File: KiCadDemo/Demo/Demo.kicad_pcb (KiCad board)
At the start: 4 copper layers, 100 x 80 mm, 66 parts, among them J1 Power, J2 22-05-7025, J3 22-05-7025, J4 22-05-7025, J5 22-05-7025, J6 Comm, J7 USB_B_Mini, J8 Debug, M1 BSS84, M2 BSS84, SW1 Reset, U1 TSR_1-2450, U2 UA78M33, U3 STM32F103CBT6, U4 DS1822-PAR, U5 MAX3486, U6 74LS06, X1 8 MHz

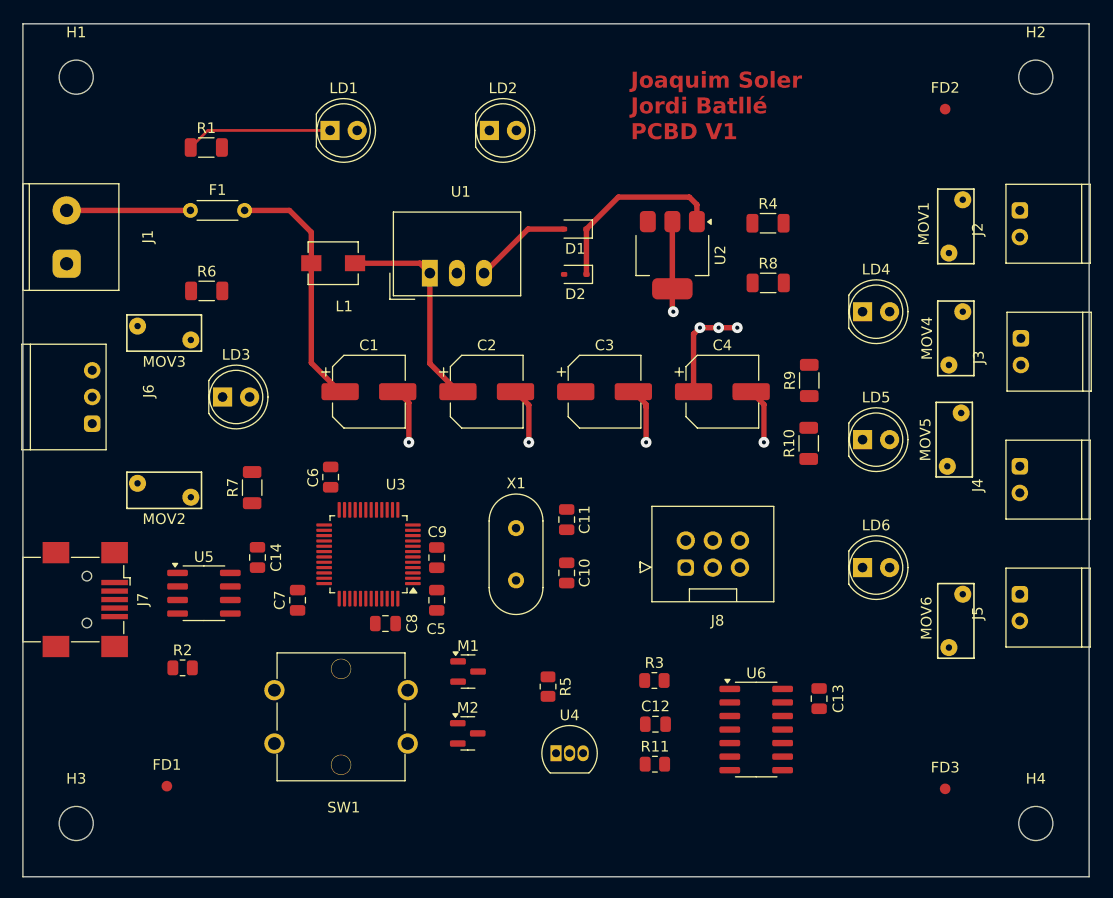
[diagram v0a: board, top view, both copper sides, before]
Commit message: Moodify component names and text label
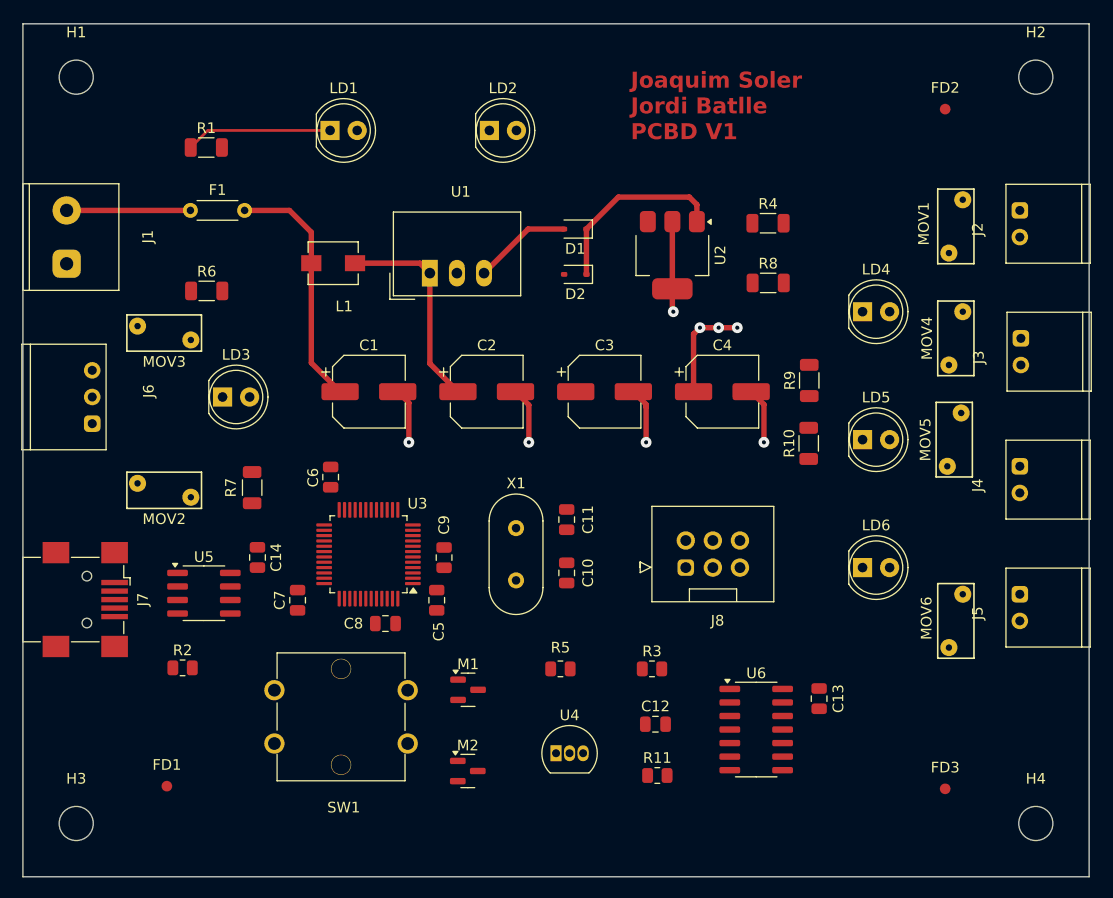
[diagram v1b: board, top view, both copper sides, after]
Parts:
- moved M2 3.53 mm to (141.7, 120.1)
- moved R5 2.03 mm to (150.4, 110.5), turned to 180 degrees
- moved M1 1.71 mm to (141.8, 112.5)
- moved R3 1.11 mm to (159.0, 110.5)
- moved R11 1.08 mm to (159.5, 120.5)
- moved C9 0.69 mm to (139.5, 100.1)
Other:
- board text added: "Joaquim Soler Jordi Batlle PCBD V1"
- board text removed: "Joaquim Soler Jordi Batllé PCBD V1"
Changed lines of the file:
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@@
   )
   (footprint "Capacitor_SMD:C_0805_2012Metric" (layer "F.Cu")
-    (at 138.8125 100.0625 90)
+    (at 139.5 100.0625 90)
     (descr "Capacitor SMD 0805 (2012 Metric), square (rectangular) end terminal, IPC_7351 nominal, (Body size source: IPC-SM-782 page 76, https://www.pcb-3d.com/wordpress/wp-content/uploads/ipc-sm-782a_amendment_1_and_2.pdf, https://docs.google.com/spreadsheets/d/1BsfQQcO9C6DZCsRaXUlFlo91Tg2WpOkGARC1WS5S8t0/edit?usp=sharing), generated with kicad-footprint-generator")
     (tags "capacitor")
@@
     (property "ki_keywords" "cap capacitor")
     (attr smd)
-    (fp_text reference "C9" (at 2.4 0.05 180) (layer "F.SilkS")
+    (fp_text reference "C9" (at 3.0625 0 270) (layer "F.SilkS")
         (effects (font (size 1 1) (thickness 0.15)))
     )
-    (fp_text value "100 nF" (at 0 1.68 90) (layer "F.Fab")
+    (fp_text value "100 nF" (at 4.5625 1.5 90) (layer "F.Fab")
         (effects (font (size 1 1) (thickness 0.15)))
     )
@@
     (property "ki_keywords" "Arm Cortex-M3 STM32F1 STM32F103")
     (attr smd)
-    (fp_text reference "U3" (at -2.55 6.5375) (layer "F.SilkS")
+    (fp_text reference "U3" (at -4.5875 4.75) (layer "F.SilkS")
         (effects (font (size 1 1) (thickness 0.15)))
     )
@@
   )
   (footprint "Resistor_SMD:R_0805_2012Metric" (layer "F.Cu")
-    (at 159.275 119.44)
+    (at 159.5 120.5)
     (descr "Resistor SMD 0805 (2012 Metric), square (rectangular) end terminal, IPC_7351 nominal, (Body size source: IPC-SM-782 page 72, https://www.pcb-3d.com/wordpress/wp-content/uploads/ipc-sm-782a_amendment_1_and_2.pdf), generated with kicad-footprint-generator")
     (tags "resistor")
@@
     (property "ki_keywords" "R res resistor")
     (attr smd)
-    (fp_text reference "R7" (at 0 -1.82 90) (layer "F.SilkS")
+    (fp_text reference "R7" (at 0 -2 90) (layer "F.SilkS")
         (effects (font (size 1 1) (thickness 0.15)))
     )
-    (fp_text value "120R" (at 0 1.82 90) (layer "F.Fab")
+    (fp_text value "120R" (at 0 2 90) (layer "F.Fab")
         (effects (font (size 1 1) (thickness 0.15)))
     )
@@
     (property "ki_keywords" "cap capacitor")
     (attr smd)
-    (fp_text reference "C5" (at -2.7 -0.05 180) (layer "F.SilkS")
+    (fp_text reference "C5" (at -2.9375 0.1875 270) (layer "F.SilkS")
         (effects (font (size 1 1) (thickness 0.15)))
     )
-    (fp_text value "100 nF" (at 0 1.68 90) (layer "F.Fab")
+    (fp_text value "100 nF" (at -1.4375 2.1875 90) (layer "F.Fab")
         (effects (font (size 1 1) (thickness 0.15)))
     )
-    (fp_text user "${REFERENCE}" (at 0 0 90) (layer "F.Fab")
+    (fp_text user "${REFERENCE}" (at 0 0.625 90) (layer "F.Fab")
         (effects (font (size 0.5 0.5) (thickness 0.08)))
     )
@@
     (property "ki_keywords" "cap capacitor")
     (attr smd)
-    (fp_text reference "C10" (at 0 -1.68 90) (layer "F.SilkS")
+    (fp_text reference "C10" (at 0 -2 90) (layer "F.SilkS")
         (effects (font (size 1 1) (thickness 0.15)))
     )
-    (fp_text value "20 pF" (at 0 1.68 90) (layer "F.Fab")
+    (fp_text value "20 pF" (at 0 -3.5 90) (layer "F.Fab")
         (effects (font (size 1 1) (thickness 0.15)))
     )
@@
     (property "ki_keywords" "cap capacitor")
     (attr smd)
-    (fp_text reference "C8" (at 2.5 0 90) (layer "F.SilkS")
+    (fp_text reference "C8" (at -3 0 180) (layer "F.SilkS")
         (effects (font (size 1 1) (thickness 0.15)))
     )
@@
   )
   (footprint "Package_TO_SOT_SMD:SOT-23" (layer "F.Cu")
-    (at 141.75 110.75)
+    (at 141.75 112.46)
     (descr "SOT, 3 Pin (https://www.jedec.org/system/files/docs/to-236h.pdf variant AB), generated with kicad-footprint-generator ipc_gullwing_generator.py")
     (tags "SOT TO_SOT_SMD")
@@
   )
   (footprint "Resistor_SMD:R_0805_2012Metric" (layer "F.Cu")
-    (at 159.225 111.59)
+    (at 159 110.5)
     (descr "Resistor SMD 0805 (2012 Metric), square (rectangular) end terminal, IPC_7351 nominal, (Body size source: IPC-SM-782 page 72, https://www.pcb-3d.com/wordpress/wp-content/uploads/ipc-sm-782a_amendment_1_and_2.pdf), generated with kicad-footprint-generator")
     (tags "resistor")
@@
     (property "ki_keywords" "cap capacitor")
     (attr smd)
-    (fp_text reference "C11" (at 0 -1.68 90) (layer "F.SilkS")
+    (fp_text reference "C11" (at 0 -2 90) (layer "F.SilkS")
         (effects (font (size 1 1) (thickness 0.15)))
     )
-    (fp_text value "20 pF" (at 0 1.68 90) (layer "F.Fab")
+    (fp_text value "20 pF" (at 0 -3.5 90) (layer "F.Fab")
         (effects (font (size 1 1) (thickness 0.15)))
     )
@@
   )
   (footprint "Resistor_SMD:R_0805_2012Metric" (layer "F.Cu")
-    (at 149.25 112.1625 -90)
+    (at 150.4125 110.5 180)
     (descr "Resistor SMD 0805 (2012 Metric), square (rectangular) end terminal, IPC_7351 nominal, (Body size source: IPC-SM-782 page 72, https://www.pcb-3d.com/wordpress/wp-content/uploads/ipc-sm-782a_amendment_1_and_2.pdf), generated with kicad-footprint-generator")
     (tags "resistor")
@@
     (property "ki_keywords" "R res resistor")
     (attr smd)
-    (fp_text reference "R5" (at 0 -1.65 90) (layer "F.SilkS")
+    (fp_text reference "R5" (at 0 2) (layer "F.SilkS")
         (effects (font (size 1 1) (thickness 0.15)))
     )
-    (fp_text value "4k7" (at 0 1.65 90) (layer "F.Fab")
+    (fp_text value "4k7" (at 0 -2) (layer "F.Fab")
         (effects (font (size 1 1) (thickness 0.15)))
     )
-    (fp_text user "${REFERENCE}" (at 0 0.625 90) (layer "F.Fab")
+    (fp_text user "${REFERENCE}" (at 0 0.625) (layer "F.Fab")
         (effects (font (size 0.5 0.5) (thickness 0.08)))
     )
@@
     (fp_line (start 1 0.625) (end -1 0.625)
       (stroke (width 0.1) (type solid)) (layer "F.Fab"))
-    (pad "1" smd roundrect (at -0.9125 0 270) (size 1.025 1.4) (layers "F.Cu" "F.Paste" "F.Mask") (roundrect_rratio 0.243902439)
+    (pad "1" smd roundrect (at -0.9125 0 180) (size 1.025 1.4) (layers "F.Cu" "F.Paste" "F.Mask") (roundrect_rratio 0.243902439)
       (net 6 "+3V3") (pintype "passive"))
-    (pad "2" smd roundrect (at 0.9125 0 270) (size 1.025 1.4) (layers "F.Cu" "F.Paste" "F.Mask") (roundrect_rratio 0.243902439)
+    (pad "2" smd roundrect (at 0.9125 0 180) (size 1.025 1.4) (layers "F.Cu" "F.Paste" "F.Mask") (roundrect_rratio 0.243902439)
       (net 13 "DQ") (pintype "passive"))
     (model "${KICAD6_3DMODEL_DIR}/Resistor_SMD.3dshapes/R_0805_2012Metric.wrl"
@@
   )
   (footprint "Package_TO_SOT_SMD:SOT-23" (layer "F.Cu")
-    (at 141.725 116.55)
+    (at 141.725 120.08)
     (descr "SOT, 3 Pin (https://www.jedec.org/system/files/docs/to-236h.pdf variant AB), generated with kicad-footprint-generator ipc_gullwing_generator.py")
     (tags "SOT TO_SOT_SMD")
@@
   (gr_line (start 100 130) (end 200 130)
     (stroke (width 0.05) (type default)) (layer "Edge.Cuts"))
-  (gr_text "Joaquim Soler\nJordi Batllé\nPCBD V1\n" (at 157 61) (layer "F.Cu")
+  (gr_text "Joaquim Soler\nJordi Batlle\nPCBD V1\n" (at 157 61) (layer "F.Cu")
     (effects (font (size 1.5 1.5) (thickness 0.3) bold) (justify left bottom))
   )

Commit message: Add files via upload
Plots generated.
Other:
- board text added: "Jordi Batlle Joaquim Soler PCB Board Demo v1.0"
- board text removed: "Joaquim Soler Jordi Batlle PCBD V1"
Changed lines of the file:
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@@
       (drillshape 0)
       (scaleselection 1)
-      (outputdirectory "")
+      (outputdirectory "Place/")
     )
   )
@@
   (gr_line (start 100 130) (end 200 130)
     (stroke (width 0.05) (type default)) (layer "Edge.Cuts"))
-  (gr_text "Joaquim Soler\nJordi Batlle\nPCBD V1\n" (at 157 61) (layer "F.Cu")
-    (effects (font (size 1.5 1.5) (thickness 0.3) bold) (justify left bottom))
+  (gr_text "Jordi Batlle\nJoaquim Soler\nPCB Board Demo v1.0" (at 154.41 58.54) (layer "F.SilkS")
+    (effects (font (size 1.5 1.5) (thickness 0.2)) (justify left bottom))
   )
   (segment (start 127.04875 81.79875) (end 129.75 84.5) (width 0.508) (layer "F.Cu") (net 1))

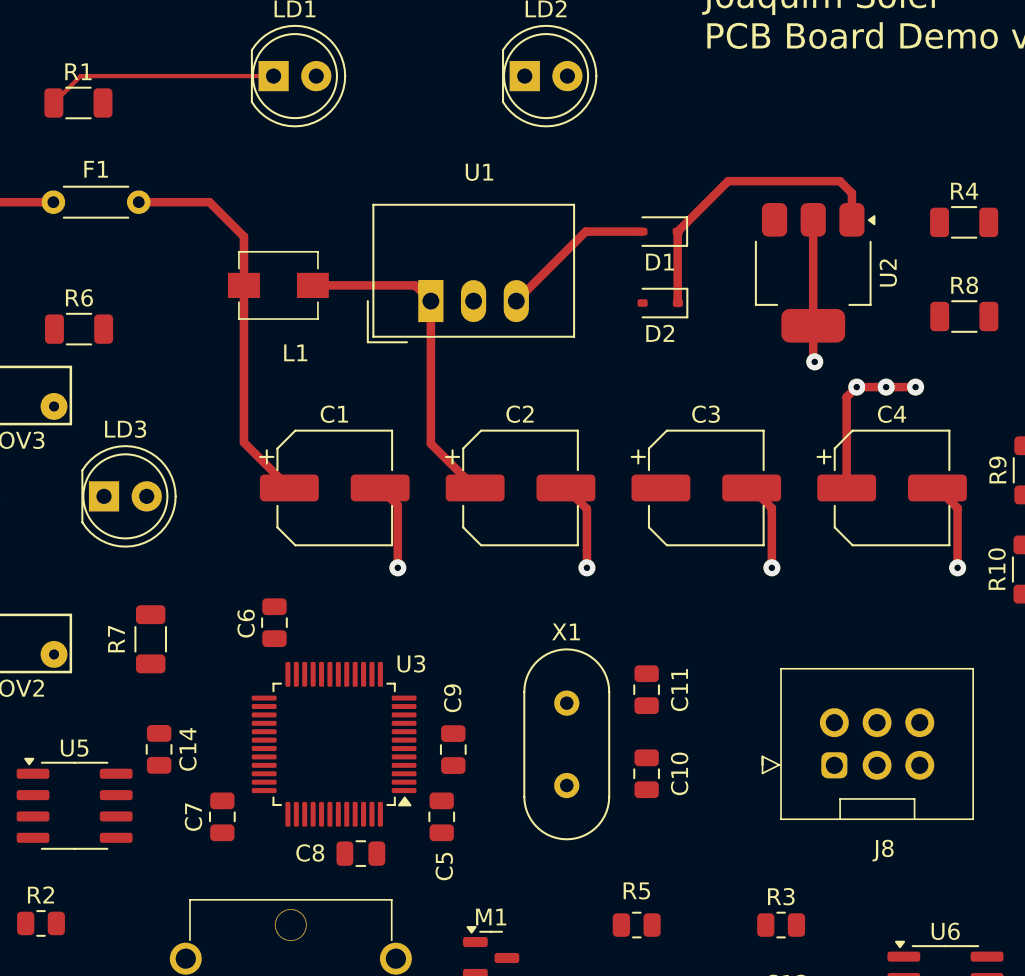
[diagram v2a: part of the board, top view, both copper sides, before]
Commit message: Start of the routing
Power lines routed. MCU coupling capacitors routed and also oscillator.
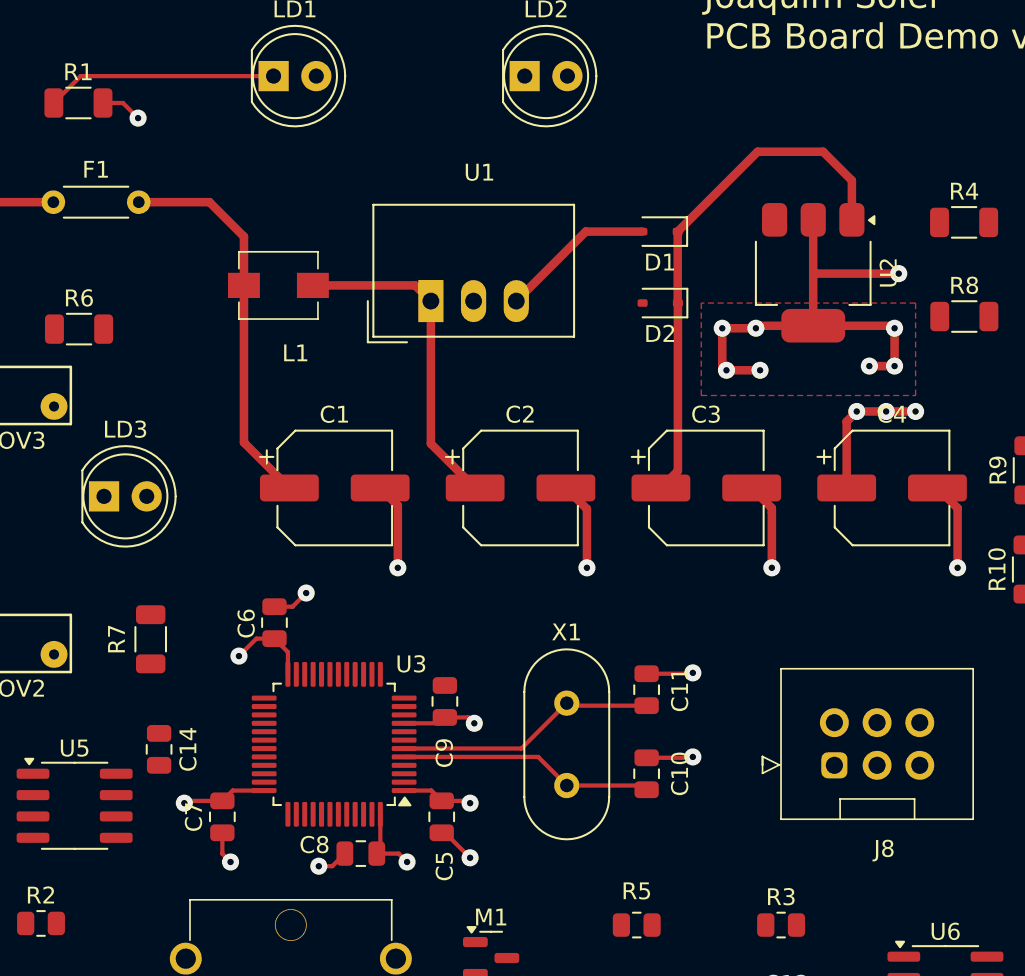
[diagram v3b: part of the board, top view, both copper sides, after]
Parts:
- moved C9 2.91 mm to (139.0, 97.2), turned to -90 degrees
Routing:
- net GND: track 29.9 -> 67.9 mm, vias 5 -> 19
- net +3V3: track 0.00 -> 23.2 mm, vias 0 -> 5
- net Net-(U3-PD1): track 0.00 -> 15.6 mm
- net Net-(U3-PD0): track 0.00 -> 15.2 mm
- net /supply/pwr5: track 17.7 -> 31.1 mm
- net +3.3V: track 9.75 -> 8.30 mm
- added copper zone on F.Cu, net GND

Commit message: Follow routing
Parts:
- moved M2 50.7 mm to (122.8, 73.1), turned to 180 degrees
- moved U5 12.2 mm to (121.0, 91.9), turned to 180 degrees
- moved R7 7.47 mm to (114.2, 92.1)
- moved MOV2 7.00 mm to (103.8, 93.8)
- moved LD3 4.65 mm to (122.0, 81.7)
- moved C14 4.28 mm to (120.8, 96.0), turned to 0 degrees
- moved C6 0.79 mm to (129.7, 92.5), turned to 180 degrees
- moved R5 0.33 mm to (150.4, 110.2)
- moved C7 0.32 mm to (125.6, 104.3)
- turned R3 to 180 degrees
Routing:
- net NRST: track 0.00 -> 100.1 mm, vias 0 -> 1
- net SWDIO: track 0.00 -> 58.3 mm
- net SWCLK: track 0.00 -> 41.4 mm
- net DQ: track 0.00 -> 36.1 mm, vias 0 -> 2
- net TX: track 0.00 -> 34.8 mm, vias 0 -> 2
- net GATE: track 0.00 -> 23.2 mm, vias 0 -> 2
- net USB_DP: track 0.00 -> 20.9 mm
- net USB_DM: track 0.00 -> 20.8 mm
- net Net-(J6-Pin_3): track 0.00 -> 19.8 mm
- net Net-(J6-Pin_1): track 0.00 -> 19.5 mm
- net RX: track 0.00 -> 16.2 mm
- net DIR: track 0.00 -> 13.7 mm, vias 0 -> 2
- net Net-(LD3-A): track 0.00 -> 10.4 mm
- net Net-(M2-D): track 0.00 -> 7.50 mm
- net +3V3: track 23.2 -> 21.1 mm
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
